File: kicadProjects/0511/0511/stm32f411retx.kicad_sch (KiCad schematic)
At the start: 21 parts, among them U2 STM32F411RETx, Y1 32.768KHz, Y2 8MHz

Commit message: placed components around stm32f411rx
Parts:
- Y2: footprint Crystal:Crystal_SMD_3215-2Pin_3.2x1.5mm -> Crystal:Crystal_SMD_3225-4Pin_3.2x2.5mm
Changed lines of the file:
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@@
 			)
 		)
-		(property "Footprint" "Crystal:Crystal_SMD_3215-2Pin_3.2x1.5mm"
+		(property "Footprint" "Crystal:Crystal_SMD_3225-4Pin_3.2x2.5mm"
 			(at 147.32 110.49 0)
 			(effects

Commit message: ended pplacement stm32 compoenents
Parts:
- BTN_NRST_STM1: footprint Button_Switch_Keyboard:SW_Cherry_MX_1.00u_PCB -> Button_Switch_SMD:SW_SPST_TL3342
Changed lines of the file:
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@@
 			)
 		)
-		(property "Footprint" "Button_Switch_Keyboard:SW_Cherry_MX_1.00u_PCB"
+		(property "Footprint" "Button_Switch_SMD:SW_SPST_TL3342"
 			(at 125.73 142.24 0)
 			(effects

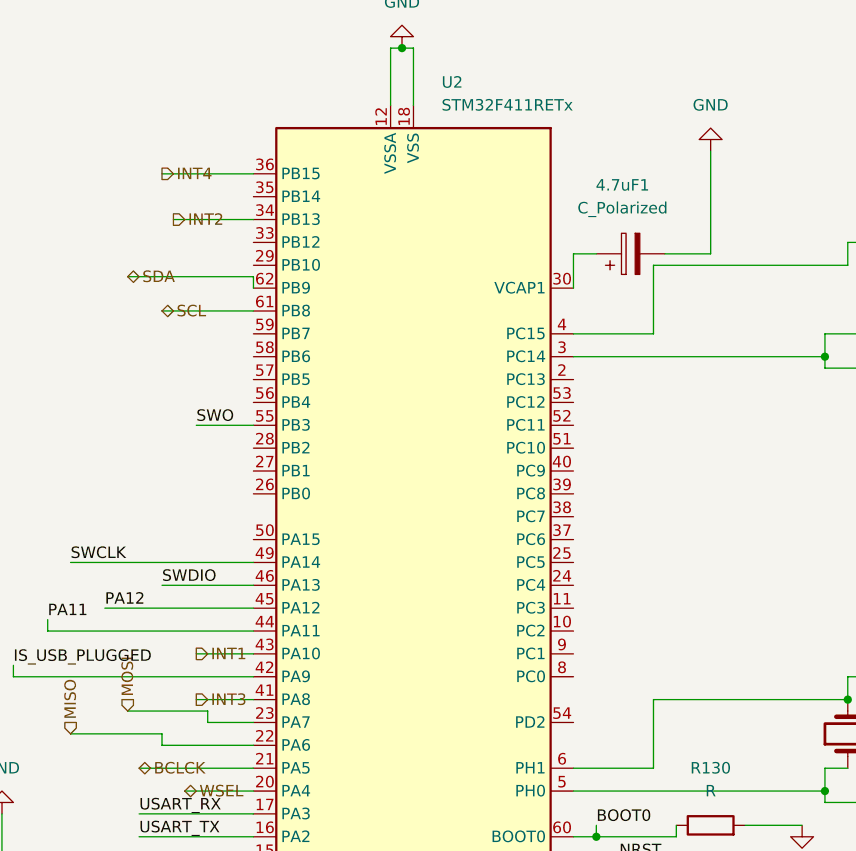
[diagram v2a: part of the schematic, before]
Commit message: added B port interruptions, updated schem and pcb
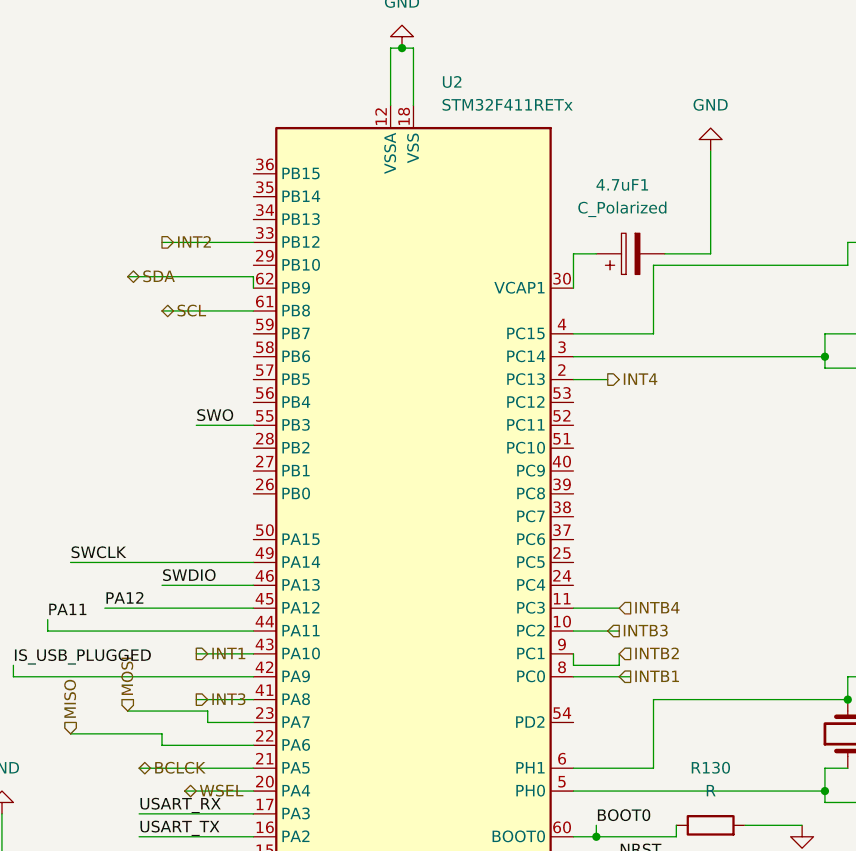
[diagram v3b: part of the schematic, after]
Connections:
- net INT2: now also U2.33 (PB12); no longer U2.34 (PB13)
- net INT4: now also U2.2 (PC13); no longer U2.36 (PB15)
- net INTB3: now reaches U2.10 (PC2)
- net INTB4: now reaches U2.11 (PC3)
- net INTB1: now reaches U2.8 (PC0)
- net INTB2: now reaches U2.9 (PC1)
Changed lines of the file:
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@@
+	(wire
+		(pts
+			(xy 116.84 96.52) (xy 121.92 96.52)
+		)
+		(stroke
+			(width 0)
+			(type default)
+		)
+	)
 	(wire
 		(pts
@@
 	(wire
 		(pts
-			(xy 71.12 48.26) (xy 81.28 48.26)
+			(xy 121.92 102.87) (xy 116.84 102.87)
 		)
 		(stroke
@@
 	(wire
 		(pts
-			(xy 72.39 53.34) (xy 81.28 53.34)
-		)
-		(stroke
-			(width 0)
-			(type default)
-		)
-	)
-	(wire
-		(pts
 			(xy 147.32 104.14) (xy 147.32 106.68)
 		)
@@
 	(wire
 		(pts
+			(xy 71.12 55.88) (xy 81.28 55.88)
+		)
+		(stroke
+			(width 0)
+			(type default)
+		)
+	)
+	(wire
+		(pts
 			(xy 167.64 69.85) (xy 167.64 60.96)
 		)
@@
 	(wire
 		(pts
+			(xy 116.84 102.87) (xy 116.84 101.6)
+		)
+		(stroke
+			(width 0)
+			(type default)
+		)
+	)
+	(wire
+		(pts
 			(xy 81.28 93.98) (xy 71.12 93.98)
 		)
@@
 	(wire
 		(pts
+			(xy 116.84 104.14) (xy 123.19 104.14)
+		)
+		(stroke
+			(width 0)
+			(type default)
+		)
+	)
+	(wire
+		(pts
+			(xy 116.84 71.12) (xy 120.65 71.12)
+		)
+		(stroke
+			(width 0)
+			(type default)
+		)
+	)
+	(wire
+		(pts
 			(xy 125.73 106.68) (xy 125.73 114.3)
 		)
@@
 	(wire
 		(pts
+			(xy 116.84 99.06) (xy 121.92 99.06)
+		)
+		(stroke
+			(width 0)
+			(type default)
+		)
+	)
+	(wire
+		(pts
 			(xy 71.12 111.76) (xy 81.28 111.76)
 		)
@@
 		(pts
 			(xy 38.1 135.89) (xy 40.64 135.89)
+		)
+		(stroke
+			(width 0)
+			(type default)
+		)
+	)
+	(wire
+		(pts
+			(xy 121.92 101.6) (xy 121.92 102.87)
 		)
 		(stroke
@@
 		)
 	)
+	(hierarchical_label "INTB4"
+		(shape input)
+		(at 121.92 96.52 0)
+		(effects
+			(font
+				(size 1.27 1.27)
+			)
+			(justify left)
+		)
+	)
 	(hierarchical_label "INT4"
 		(shape output)
-		(at 71.12 48.26 0)
+		(at 120.65 71.12 0)
 		(effects
 			(font
@@
 		)
 	)
+	(hierarchical_label "INTB3"
+		(shape input)
+		(at 120.65 99.06 0)
+		(effects
+			(font
+				(size 1.27 1.27)
+			)
+			(justify left)
+		)
+	)
 	(hierarchical_label "FSR"
 		(shape bidirectional)
@@
 	(hierarchical_label "INT2"
 		(shape output)
-		(at 72.39 53.34 0)
+		(at 71.12 55.88 0)
 		(effects
 			(font
@@
 		(effects
 			(font
+				(size 1.27 1.27)
+			)
+			(justify left)
+		)
+	)
+	(hierarchical_label "INTB1"
+		(shape input)
+		(at 121.92 104.14 0)
+		(effects
+			(font
+				(size 1.27 1.27)
+			)
+			(justify left)
+		)
+	)
+	(hierarchical_label "INTB2"
+		(shape input)
+		(at 121.92 101.6 0)
+		(effects
+			(font

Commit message: ajout empreinte quarty mhz
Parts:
- Y2: footprint Crystal:Crystal_SMD_3225-4Pin_3.2x2.5mm -> Project:XTAL_ABLS2-8.000MHZ-D4Y-T
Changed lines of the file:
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@@
 			)
 		)
-		(property "Footprint" "Crystal:Crystal_SMD_3225-4Pin_3.2x2.5mm"
+		(property "Footprint" "Project:XTAL_ABLS2-8.000MHZ-D4Y-T"
 			(at 147.32 110.49 0)
 			(effects

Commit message: correctif adafruit component
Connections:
- net MISO: no longer names the net of U2.22 (PA6)
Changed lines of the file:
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@@
-	(wire
-		(pts
-			(xy 60.96 110.49) (xy 71.12 110.49)
-		)
-		(stroke
-			(width 0)
-			(type default)
-		)
-	)
 	(wire
 		(pts
@@
 	(wire
 		(pts
-			(xy 71.12 110.49) (xy 71.12 111.76)
-		)
-		(stroke
-			(width 0)
-			(type default)
-		)
-	)
-	(wire
-		(pts
 			(xy 132.08 57.15) (xy 132.08 45.72)
 		)
@@
 		(pts
 			(xy 116.84 99.06) (xy 121.92 99.06)
-		)
-		(stroke
-			(width 0)
-			(type default)
-		)
-	)
-	(wire
-		(pts
-			(xy 71.12 111.76) (xy 81.28 111.76)
 		)
 		(stroke
@@
 		(effects
 			(font
-				(size 1.27 1.27)
-			)
-			(justify left)
-		)
-	)
-	(hierarchical_label "MISO"
-		(shape input)
-		(at 60.96 110.49 90)
-		(effects
-			(font

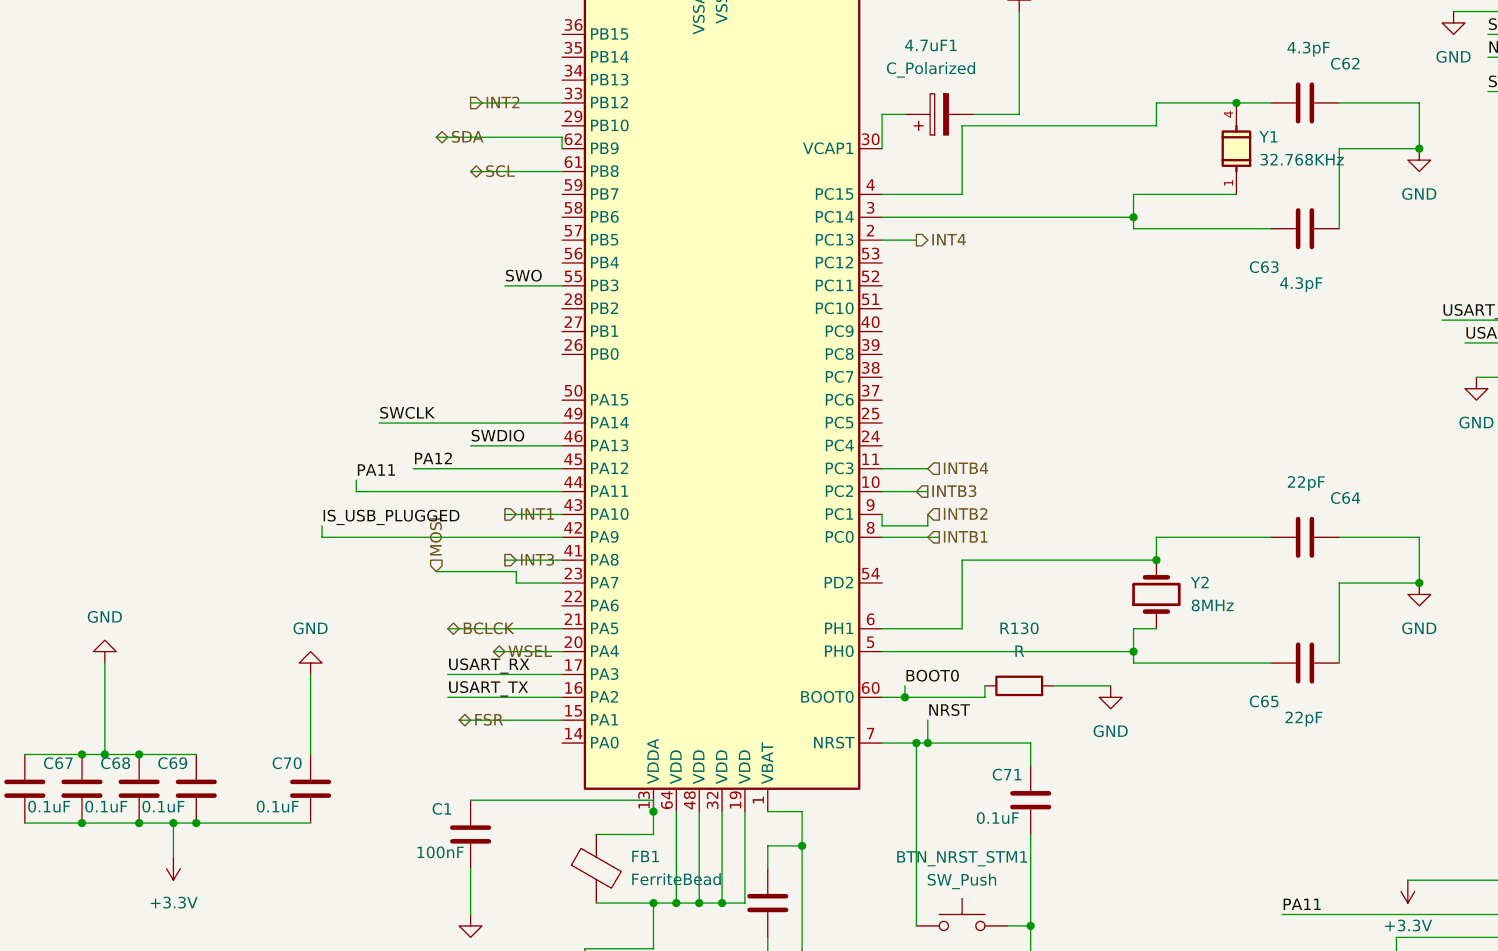
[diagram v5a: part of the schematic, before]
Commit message: added push buttons
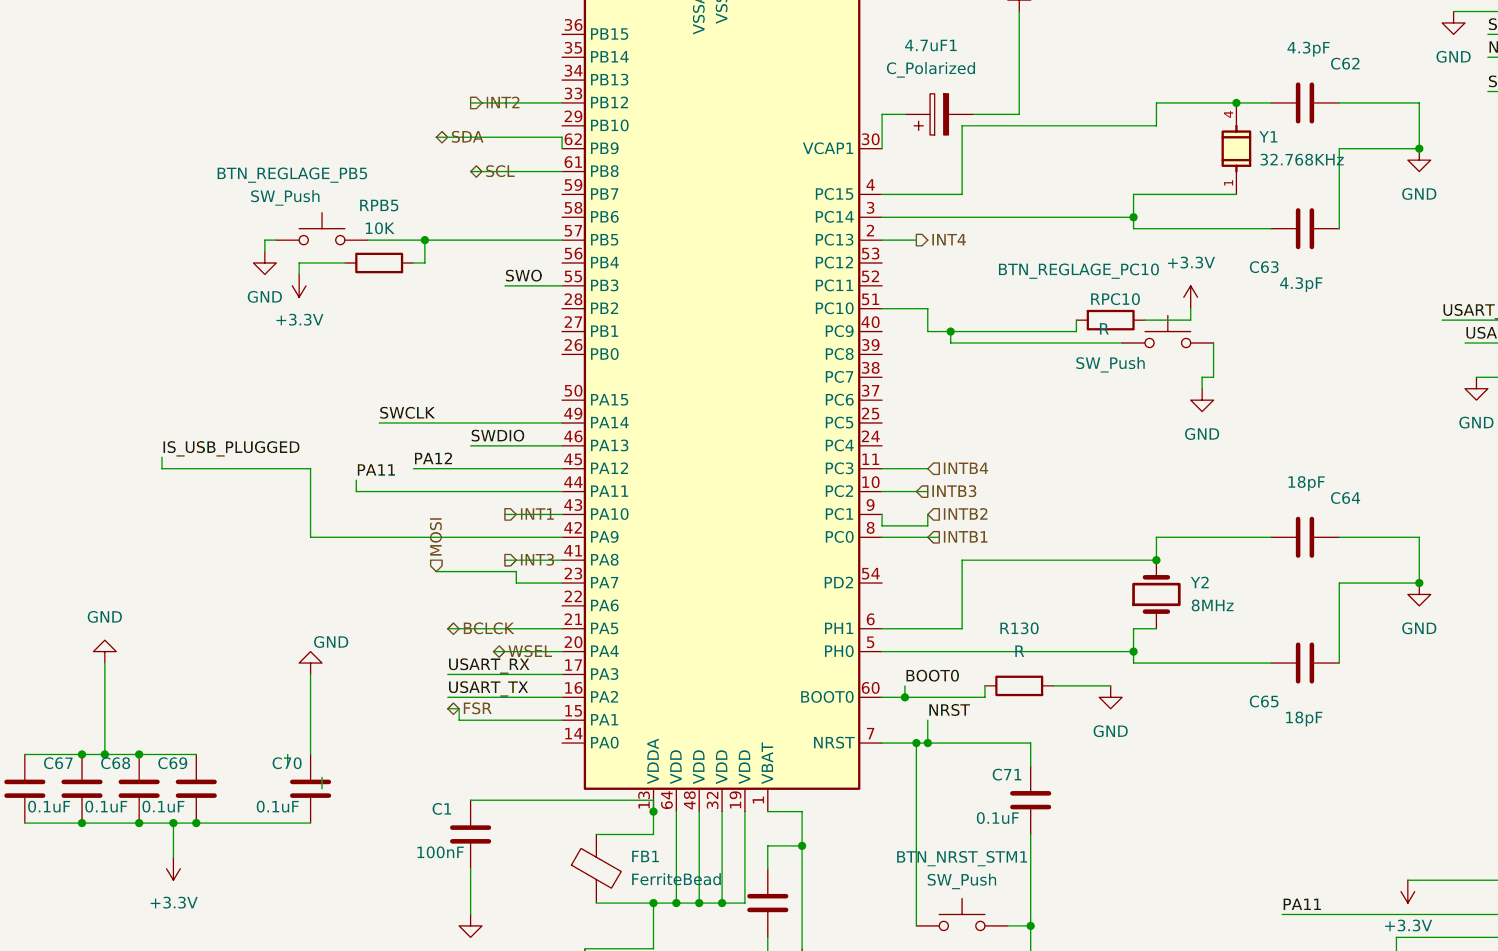
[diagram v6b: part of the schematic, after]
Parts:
- added BTN_REGLAGE_PB5, BTN_REGLAGE_PC10: SW_Push, Button_Switch_SMD:SW_SPST_TL3342, symbol Switch:SW_Push
- added RPB5: 10K, Resistor_SMD:R_0603_1608Metric, symbol Device:R
- added RPC10: R, Resistor_SMD:R_0603_1608Metric, symbol Device:R
- C64, C65: value 22pF -> 18pF
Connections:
- net +3.3V: now also RPB5.1, RPC10.1
- net GND: now also BTN_REGLAGE_PB5.1, BTN_REGLAGE_PC10.2
- net at U2.51 (PC10): now also BTN_REGLAGE_PC10.1, RPC10.2
- net at U2.57 (PB5): now also BTN_REGLAGE_PB5.2, RPB5.2

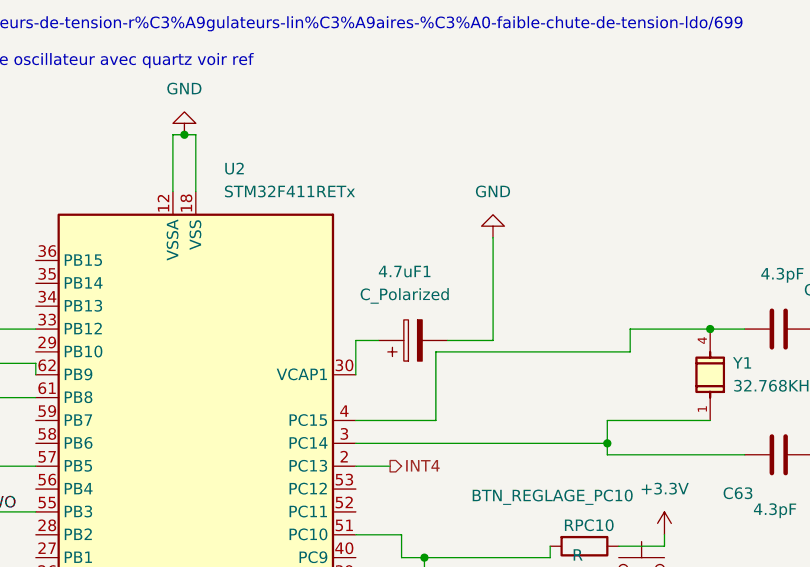
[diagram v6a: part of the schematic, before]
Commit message: correctifs, ajout sérigraphie test points
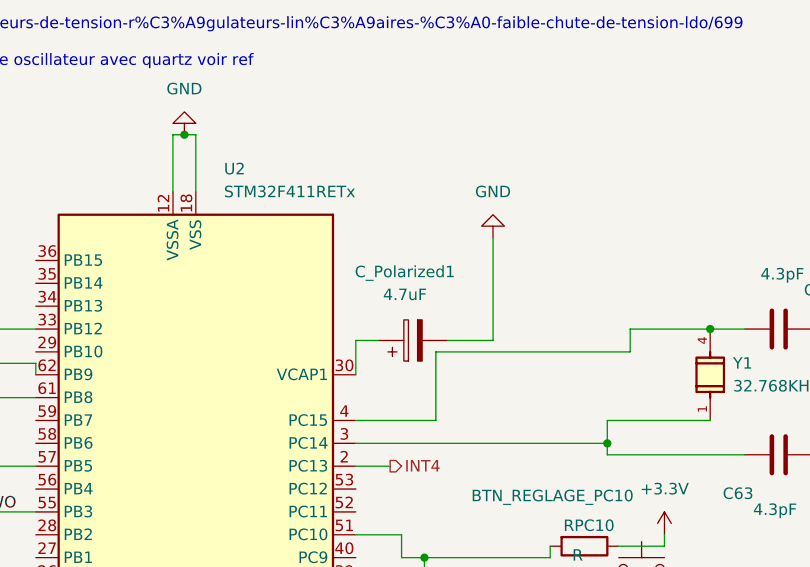
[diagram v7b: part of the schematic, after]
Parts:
- C_Polarized1: renamed from 4.7uF1; value C_Polarized -> 4.7uF
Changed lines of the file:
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@@
 		(dnp no)
 		(fields_autoplaced yes)
-		(property "Reference" "4.7uF1"
+		(property "Reference" "C_Polarized1"
 			(at 122.301 49.53 90)
 			(effects
@@
 			)
 		)
-		(property "Value" "C_Polarized"
+		(property "Value" "4.7uF"
 			(at 122.301 52.07 90)
 			(effects
@@
 			(project ""
 				(path "/2c0b0e0d-c5e7-48b7-93bb-9be1941509af/7f025c79-ea20-4013-a71e-871359ae3c80"
-					(reference "4.7uF1")
+					(reference "C_Polarized1")
 					(unit 1)
 				)

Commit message: correctifs valeurs manquantes
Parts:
- C72: value C -> 1uF
- LDOCout1: renamed from C68; value 0.1uF -> 1uF
- R130, RPC10: value R -> 10K
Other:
- moved on the sheet: C70
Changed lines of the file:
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@@
 	(wire
 		(pts
+			(xy 53.34 127) (xy 53.34 119.38)
+		)
+		(stroke
+			(width 0)
+			(type default)
+		)
+	)
+	(wire
+		(pts
 			(xy 68.58 119.38) (xy 81.28 119.38)
 		)
@@
 	(wire
 		(pts
+			(xy 48.26 127) (xy 53.34 127)
+		)
+		(stroke
+			(width 0)
+			(type default)
+		)
+	)
+	(wire
+		(pts
 			(xy 160.02 104.14) (xy 147.32 104.14)
 		)
@@
 	(wire
 		(pts
-			(xy 54.61 130.81) (xy 54.61 132.08)
-		)
-		(stroke
-			(width 0)
-			(type default)
-		)
-	)
-	(wire
-		(pts
 			(xy 27.94 135.89) (xy 34.29 135.89)
 		)
@@
 	(wire
 		(pts
-			(xy 40.64 135.89) (xy 53.34 135.89)
+			(xy 50.8 133.35) (xy 48.26 133.35)
 		)
 		(stroke
@@
 	(wire
 		(pts
+			(xy 50.8 133.35) (xy 50.8 135.89)
+		)
+		(stroke
+			(width 0)
+			(type default)
+		)
+	)
+	(wire
+		(pts
 			(xy 151.13 78.74) (xy 151.13 80.01)
 		)
@@
 	(wire
 		(pts
-			(xy 53.34 119.38) (xy 53.34 128.27)
+			(xy 50.8 135.89) (xy 40.64 135.89)
+		)
+		(stroke
+			(width 0)
+			(type default)
+		)
+	)
+	(wire
+		(pts
+			(xy 48.26 127) (xy 48.26 125.73)
 		)
 		(stroke
@@
 	(wire
 		(pts
-			(xy 50.8 129.54) (xy 50.8 128.27)
-		)
-		(stroke
-			(width 0)
-			(type default)
-		)
-	)
-	(wire
-		(pts
 			(xy 68.58 121.92) (xy 81.28 121.92)
 		)
@@
 	(symbol
 		(lib_id "Device:C")
-		(at 53.34 132.08 0)
+		(at 48.26 129.54 0)
 		(unit 1)
 		(exclude_from_sim no)
@@
 		(dnp no)
 		(property "Reference" "C70"
-			(at 49.022 129.286 0)
+			(at 49.784 134.62 0)
 			(effects
 				(font
@@
 		)
 		(property "Value" "0.1uF"
-			(at 47.244 134.112 0)
+			(at 42.164 131.572 0)
 			(effects
 				(font
@@
 		)
 		(property "Footprint" "Capacitor_SMD:C_0603_1608Metric"
-			(at 54.3052 135.89 0)
+			(at 49.2252 133.35 0)
 			(effects
 				(font
@@
 		)
 		(property "Datasheet" "~"
-			(at 53.34 132.08 0)
+			(at 48.26 129.54 0)
 			(effects
 				(font
@@
 		)
 		(property "Description" "Unpolarized capacitor"
-			(at 53.34 132.08 0)
+			(at 48.26 129.54 0)
 			(effects
 				(font
@@
 			)
 		)
-		(property "Value" "R"
+		(property "Value" "10K"
 			(at 141.478 81.026 90)
 			(effects
@@
 		(on_board yes)
 		(dnp no)
-		(fields_autoplaced yes)
 		(property "Reference" "R130"
 			(at 132.08 114.3 90)
@@
 			)
 		)
-		(property "Value" "R"
+		(property "Value" "10K"
 			(at 132.08 116.84 90)
 			(effects
@@
 		(on_board yes)
 		(dnp no)
-		(property "Reference" "C68"
-			(at 29.972 129.286 0)
+		(property "Reference" "LDOCout1"
+			(at 30.226 125.222 0)
 			(effects
 				(font
@@
 			)
 		)
-		(property "Value" "0.1uF"
+		(property "Value" "1uF"
 			(at 28.194 134.112 0)
 			(effects
@@
 			(project "0511"
 				(path "/2c0b0e0d-c5e7-48b7-93bb-9be1941509af/7f025c79-ea20-4013-a71e-871359ae3c80"
-					(reference "C68")
+					(reference "LDOCout1")
 					(unit 1)
 				)
@@
 			)
 		)
-		(property "Value" "C"
+		(property "Value" "1uF"
 			(at 101.6 150.876 0)
 			(effects
